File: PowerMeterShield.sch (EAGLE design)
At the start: 16 parts, among them IC1 MCP3426A0-E/SN, IC2 INA138

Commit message: Added DC-DC converter to isolate circuit; still missing optocouplers and differential voltage measurement
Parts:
- added DC1: VA-0505S, dc-dc-converter:VA-0505S
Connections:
- new net +5V: DC1.+VIN, JP3.4
- new net +5V/2: DC1.+VOUT
- new net GNDI: DC1.-VOUT
- net GND: now also DC1.-VIN
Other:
- moved on the sheet: JP3, JP4
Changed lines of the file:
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@@
 <attribute name="PRICE_10" value="1.21"/>
 </part>
-<part name="GND3" library="supply1" deviceset="GND" device=""/>
+<part name="GND3" library="supply1" deviceset="GNDI" device=""/>
 <part name="R4" library="rcl" deviceset="R-EU_" device="R0805" value="200k">
 <attribute name="OC_FARNELL" value="2129299"/>
@@
 <attribute name="PRICE_100" value="0.001"/>
 </part>
-<part name="GND1" library="supply1" deviceset="GND" device=""/>
+<part name="GND1" library="supply1" deviceset="GNDI" device=""/>
 <part name="X1" library="con-wago-500" deviceset="W237-102" device="">
 <attribute name="OC_FARNELL" value="1717001"/>
@@
 <attribute name="PRICE_10" value="2.06"/>
 </part>
-<part name="GND2" library="supply1" deviceset="GND" device=""/>
+<part name="GND2" library="supply1" deviceset="GNDI" device=""/>
 <part name="JP1" library="pinhead" deviceset="PINHD-1X10" device=""/>
 <part name="JP2" library="pinhead" deviceset="PINHD-1X8" device=""/>
@@
 <attribute name="PRICE_100" value="0.005"/>
 </part>
+<part name="DC1" library="dc-dc-converter" deviceset="VA-*?" device="S" technology="0505"/>
 </parts>
 <sheets>
@@
 <attribute name="PRICE_10" x="50.8" y="83.82" size="1.27" layer="96" display="off"/>
 </instance>
-<instance part="GND3" gate="1" x="68.58" y="60.96"/>
+<instance part="GND3" gate="G$1" x="68.58" y="60.96"/>
 <instance part="R4" gate="G$1" x="68.58" y="83.82" smashed="yes" rot="R90">
 <attribute name="OC_FARNELL" x="68.58" y="83.82" size="1.27" layer="96" rot="R90" display="off"/>
@@
 <attribute name="OC_FARNELL" x="58.42" y="66.04" size="1.27" layer="96" rot="R180" display="off"/>
 </instance>
-<instance part="GND1" gate="1" x="25.4" y="71.12"/>
+<instance part="GND1" gate="G$1" x="25.4" y="71.12"/>
 <instance part="X1" gate="-1" x="17.78" y="93.98">
 <attribute name="PRICE_10" x="17.78" y="93.98" size="1.27" layer="96" display="off"/>
@@
 <attribute name="PRICE_10" x="127" y="81.28" size="1.27" layer="96" display="off"/>
 </instance>
-<instance part="GND2" gate="1" x="93.98" y="60.96"/>
+<instance part="GND2" gate="G$1" x="93.98" y="60.96"/>
 <instance part="JP1" gate="A" x="160.02" y="195.58" rot="R90"/>
 <instance part="JP2" gate="A" x="193.04" y="195.58" rot="R90"/>
-<instance part="JP3" gate="A" x="157.48" y="149.86" rot="R270"/>
-<instance part="JP4" gate="A" x="185.42" y="149.86" rot="R270"/>
+<instance part="JP3" gate="A" x="157.48" y="132.08" rot="R270"/>
+<instance part="JP4" gate="A" x="185.42" y="132.08" rot="R270"/>
 <instance part="R1" gate="G$1" x="121.92" y="175.26" smashed="yes">
 <attribute name="OC_FARNELL" x="121.92" y="175.26" size="1.27" layer="96" display="off"/>
@@
 <attribute name="OC_FARNELL" x="101.6" y="88.9" size="1.27" layer="96" rot="R270" display="off"/>
 </instance>
+<instance part="DC1" gate="G$1" x="111.76" y="132.08" rot="R180"/>
 </instances>
 <busses>
@@
 <segment>
 <pinref part="IC2" gate="G$1" pin="V-"/>
-<pinref part="GND3" gate="1" pin="GND"/>
+<pinref part="GND3" gate="G$1" pin="GNDI"/>
 <wire x1="60.96" y1="76.2" x2="68.58" y2="76.2" width="0.1524" layer="91"/>
 <wire x1="68.58" y1="76.2" x2="68.58" y2="66.04" width="0.1524" layer="91"/>
@@
 <wire x1="25.4" y1="76.2" x2="25.4" y2="73.66" width="0.1524" layer="91"/>
 <junction x="25.4" y="76.2"/>
-<pinref part="GND1" gate="1" pin="GND"/>
+<pinref part="GND1" gate="G$1" pin="GNDI"/>
 <pinref part="X1" gate="-2" pin="KL"/>
 <pinref part="X2" gate="-2" pin="KL"/>
@@
 <junction x="93.98" y="66.04"/>
 <wire x1="93.98" y1="66.04" x2="93.98" y2="63.5" width="0.1524" layer="91"/>
-<pinref part="GND2" gate="1" pin="GND"/>
+<pinref part="GND2" gate="G$1" pin="GNDI"/>
 <wire x1="93.98" y1="76.2" x2="93.98" y2="81.28" width="0.1524" layer="91"/>
 <junction x="93.98" y="76.2"/>
@@
 <segment>
 <pinref part="JP3" gate="A" pin="3"/>
-<wire x1="162.56" y1="152.4" x2="162.56" y2="157.48" width="0.1524" layer="91"/>
+<wire x1="162.56" y1="134.62" x2="162.56" y2="139.7" width="0.1524" layer="91"/>
 <pinref part="JP3" gate="A" pin="2"/>
-<wire x1="165.1" y1="152.4" x2="165.1" y2="157.48" width="0.1524" layer="91"/>
-<wire x1="162.56" y1="157.48" x2="165.1" y2="157.48" width="0.1524" layer="91"/>
-<wire x1="165.1" y1="157.48" x2="165.1" y2="160.02" width="0.1524" layer="91"/>
-<junction x="165.1" y="157.48"/>
-<label x="165.1" y="160.02" size="1.27" layer="95" rot="R90" xref="yes"/>
+<wire x1="165.1" y1="134.62" x2="165.1" y2="139.7" width="0.1524" layer="91"/>
+<wire x1="162.56" y1="139.7" x2="165.1" y2="139.7" width="0.1524" layer="91"/>
+<wire x1="165.1" y1="139.7" x2="165.1" y2="142.24" width="0.1524" layer="91"/>
+<junction x="165.1" y="139.7"/>
+<label x="165.1" y="142.24" size="1.27" layer="95" rot="R90" xref="yes"/>
 </segment>
 <segment>
@@
 <wire x1="157.48" y1="193.04" x2="157.48" y2="187.96" width="0.1524" layer="91"/>
 <label x="157.48" y="187.96" size="1.27" layer="95" rot="R270" xref="yes"/>
+</segment>
+<segment>
+<pinref part="DC1" gate="G$1" pin="-VIN"/>
+<wire x1="124.46" y1="134.62" x2="127" y2="134.62" width="0.1524" layer="91"/>
+<label x="127" y="134.62" size="1.27" layer="95" xref="yes"/>
 </segment>
 </net>
@@
 <segment>
 <pinref part="JP3" gate="A" pin="7"/>
-<wire x1="152.4" y1="152.4" x2="152.4" y2="157.48" width="0.1524" layer="91"/>
-<label x="152.4" y="157.48" size="1.27" layer="95" rot="R90" xref="yes"/>
+<wire x1="152.4" y1="134.62" x2="152.4" y2="139.7" width="0.1524" layer="91"/>
+<label x="152.4" y="139.7" size="1.27" layer="95" rot="R90" xref="yes"/>
 </segment>
 <segment>
@@
 </segment>
 </net>
+<net name="+5V" class="0">
+<segment>
+<pinref part="JP3" gate="A" pin="4"/>
+<wire x1="160.02" y1="134.62" x2="160.02" y2="139.7" width="0.1524" layer="91"/>
+<label x="160.02" y="139.7" size="1.27" layer="95" rot="R90" xref="yes"/>
+</segment>
+<segment>
+<pinref part="DC1" gate="G$1" pin="+VIN"/>
+<wire x1="124.46" y1="129.54" x2="127" y2="129.54" width="0.1524" layer="91"/>
+<label x="127" y="129.54" size="1.27" layer="95" xref="yes"/>
+</segment>
+</net>
+<net name="GNDI" class="0">
+<segment>
+<pinref part="DC1" gate="G$1" pin="-VOUT"/>
+<wire x1="99.06" y1="134.62" x2="96.52" y2="134.62" width="0.1524" layer="91"/>
+<label x="96.52" y="134.62" size="1.27" layer="95" rot="R180" xref="yes"/>
+</segment>
+</net>
+<net name="+5V/2" class="0">
+<segment>
+<pinref part="DC1" gate="G$1" pin="+VOUT"/>
+<wire x1="99.06" y1="129.54" x2="96.52" y2="129.54" width="0.1524" layer="91"/>
+<label x="96.52" y="129.54" size="1.27" layer="95" rot="R180" xref="yes"/>
+</segment>
+</net>

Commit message: Added I²C isolation
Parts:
- added U1: ADUM1250ARZ, Adum1250:ADUM1250ARZ
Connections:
- new net SCLI: IC1.SCL, U1.SCL2
- new net SDAI: IC1.SDA, U1.SDA2
- net +5V/2: now also C1.1, IC1.VDD, IC2.V+, U1.VDD2
- net GND: now also U1.GND1; no longer C1.2, IC1.CH1-, IC1.CH2-, IC1.VSS, IC2.V-, R10.1, R4.1, X1-2.KL, X2-2.KL
- net GNDI: now also C1.2, IC1.CH1-, IC1.CH2-, IC1.VSS, IC2.V-, R10.1, R4.1, U1.GND2, X1-2.KL, X2-2.KL
- net IOREF: now also U1.VDD1; no longer C1.1, IC1.VDD, IC2.V+
- net SCL: now also U1.SCL1; no longer IC1.SCL
- net SDA: now also U1.SDA1; no longer IC1.SDA

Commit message: Added creepage distance of about 3mm for a bit of safety™
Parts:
- DC1: OC_FARNELL (none) -> 2079696
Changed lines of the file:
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@@
 <attribute name="PRICE_100" value="0.005"/>
 </part>
-<part name="DC1" library="dc-dc-converter" deviceset="VA-*?" device="S" technology="0505"/>
+<part name="DC1" library="dc-dc-converter" deviceset="VA-*?" device="S" technology="0505">
+<attribute name="OC_FARNELL" value="2079696"/>
+</part>
 <part name="U1" library="Adum1250" deviceset="ADUM1250ARZ" device=""/>
 </parts>

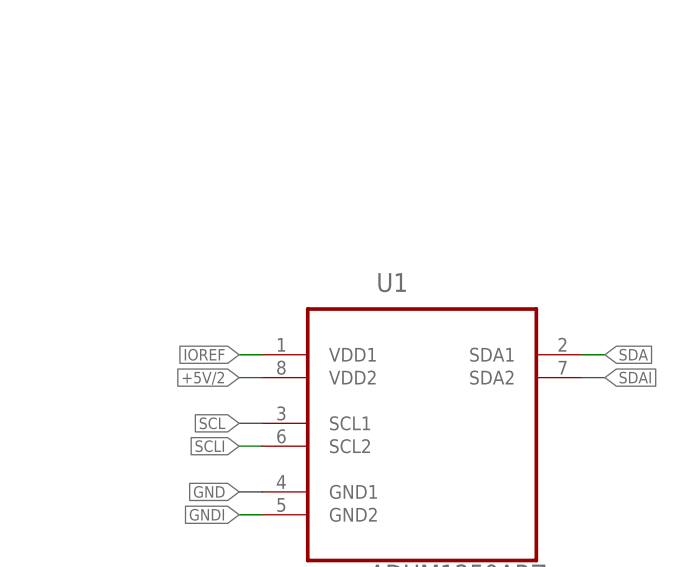
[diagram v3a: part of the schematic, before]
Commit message: Finalized design, made PCB larger in order to compensate for heigher components than the headers, so users can stack other shields on top of ours (hopefully).
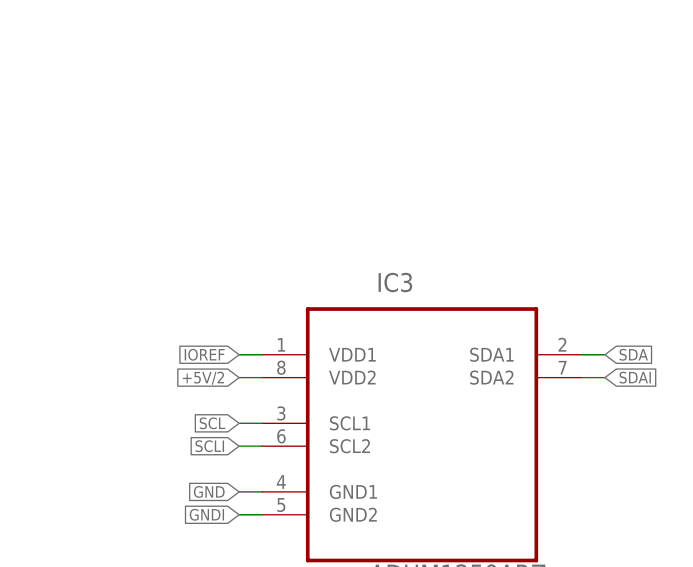
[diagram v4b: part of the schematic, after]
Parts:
- renumbered U1 to IC3
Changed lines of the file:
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@@
 <attribute name="PRICE_100" value="0.005"/>
 </part>
-<part name="DC1" library="dc-dc-converter" deviceset="VA-*?" device="S" technology="0505">
+<part name="DC1" library="dc-dc-converter" deviceset="VA-*?" device="S" technology="0505" value="VA-0505S">
 <attribute name="OC_FARNELL" value="2079696"/>
 </part>
-<part name="U1" library="Adum1250" deviceset="ADUM1250ARZ" device=""/>
+<part name="IC3" library="Adum1250" deviceset="ADUM1250ARZ" device=""/>
 </parts>
 <sheets>
@@
 </instance>
 <instance part="DC1" gate="G$1" x="111.76" y="132.08" rot="R180"/>
-<instance part="U1" gate="A" x="220.98" y="81.28"/>
+<instance part="IC3" gate="A" x="220.98" y="81.28"/>
 </instances>
 <busses>
@@
 </segment>
 <segment>
-<pinref part="U1" gate="A" pin="GND1"/>
+<pinref part="IC3" gate="A" pin="GND1"/>
 <wire x1="203.2" y1="71.12" x2="200.66" y2="71.12" width="0.1524" layer="91"/>
 <label x="200.66" y="71.12" size="1.27" layer="95" rot="R180" xref="yes"/>
@@
 </segment>
 <segment>
-<pinref part="U1" gate="A" pin="SCL1"/>
+<pinref part="IC3" gate="A" pin="SCL1"/>
 <wire x1="203.2" y1="78.74" x2="200.66" y2="78.74" width="0.1524" layer="91"/>
 <label x="200.66" y="78.74" size="1.27" layer="95" rot="R180" xref="yes"/>
@@
 </segment>
 <segment>
-<pinref part="U1" gate="A" pin="SDA1"/>
+<pinref part="IC3" gate="A" pin="SDA1"/>
 <wire x1="238.76" y1="86.36" x2="241.3" y2="86.36" width="0.1524" layer="91"/>
 <label x="241.3" y="86.36" size="1.27" layer="95" xref="yes"/>
@@
 </segment>
 <segment>
-<pinref part="U1" gate="A" pin="VDD1"/>
+<pinref part="IC3" gate="A" pin="VDD1"/>
 <wire x1="203.2" y1="86.36" x2="200.66" y2="86.36" width="0.1524" layer="91"/>
 <label x="200.66" y="86.36" size="1.27" layer="95" rot="R180" xref="yes"/>
@@
 </segment>
 <segment>
-<pinref part="U1" gate="A" pin="GND2"/>
+<pinref part="IC3" gate="A" pin="GND2"/>
 <wire x1="203.2" y1="68.58" x2="200.66" y2="68.58" width="0.1524" layer="91"/>
 <label x="200.66" y="68.58" size="1.27" layer="95" rot="R180" xref="yes"/>
@@
 </segment>
 <segment>
-<pinref part="U1" gate="A" pin="VDD2"/>
+<pinref part="IC3" gate="A" pin="VDD2"/>
 <wire x1="203.2" y1="83.82" x2="200.66" y2="83.82" width="0.1524" layer="91"/>
 <label x="200.66" y="83.82" size="1.27" layer="95" rot="R180" xref="yes"/>
@@
 </segment>
 <segment>
-<pinref part="U1" gate="A" pin="SDA2"/>
+<pinref part="IC3" gate="A" pin="SDA2"/>
 <wire x1="238.76" y1="83.82" x2="241.3" y2="83.82" width="0.1524" layer="91"/>
 <label x="241.3" y="83.82" size="1.27" layer="95" xref="yes"/>
@@
 </segment>
 <segment>
-<pinref part="U1" gate="A" pin="SCL2"/>
+<pinref part="IC3" gate="A" pin="SCL2"/>
 <wire x1="203.2" y1="76.2" x2="200.66" y2="76.2" width="0.1524" layer="91"/>
 <label x="200.66" y="76.2" size="1.27" layer="95" rot="R180" xref="yes"/>

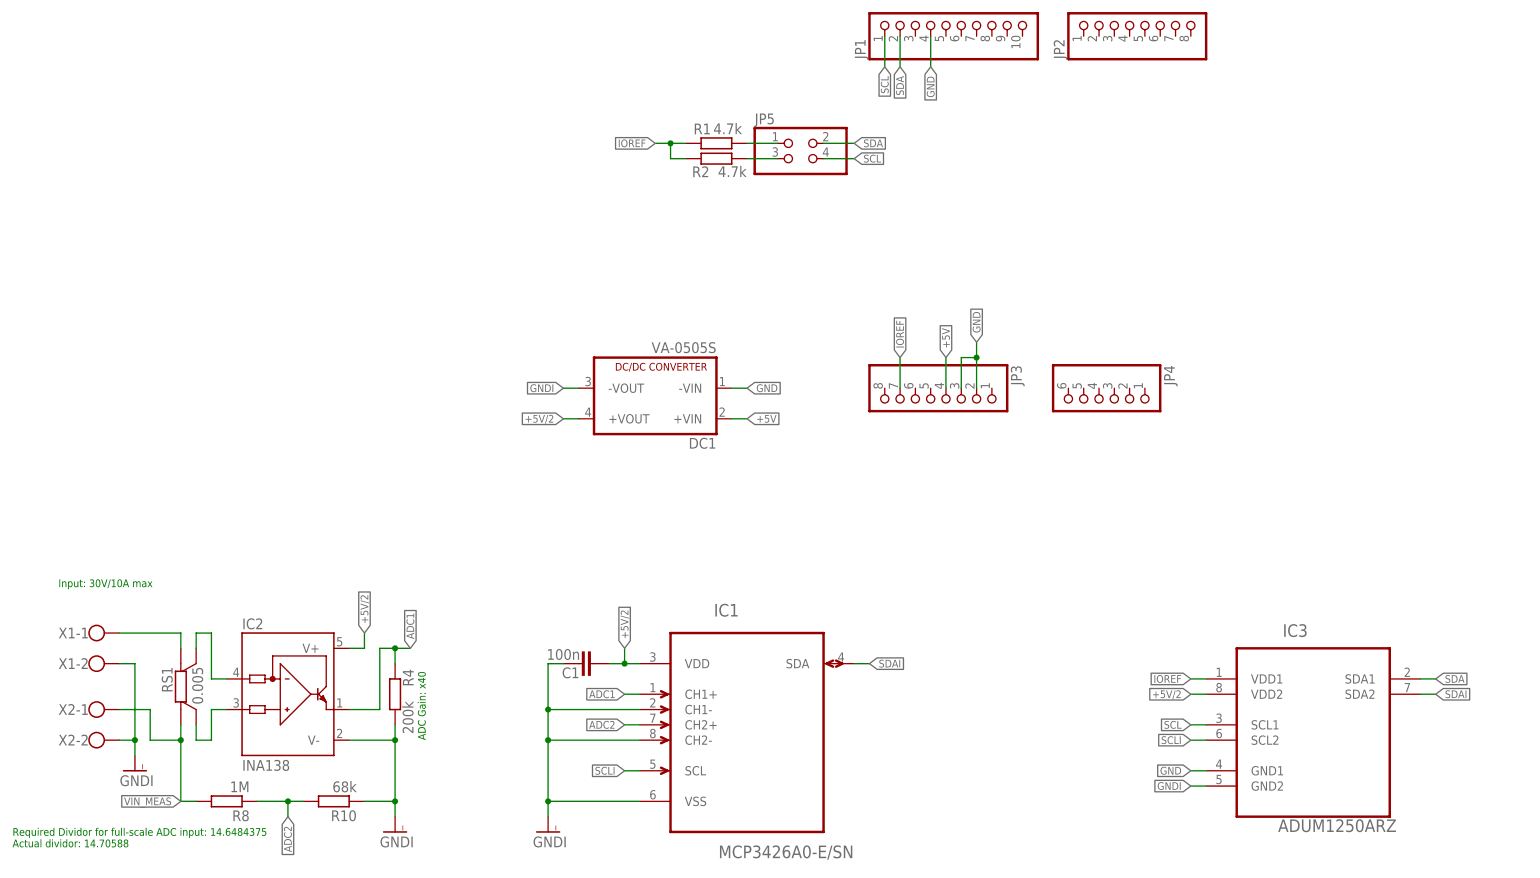
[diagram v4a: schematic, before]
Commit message: Added port names to silkscreen, added I²C pullups for the internal I²C bus
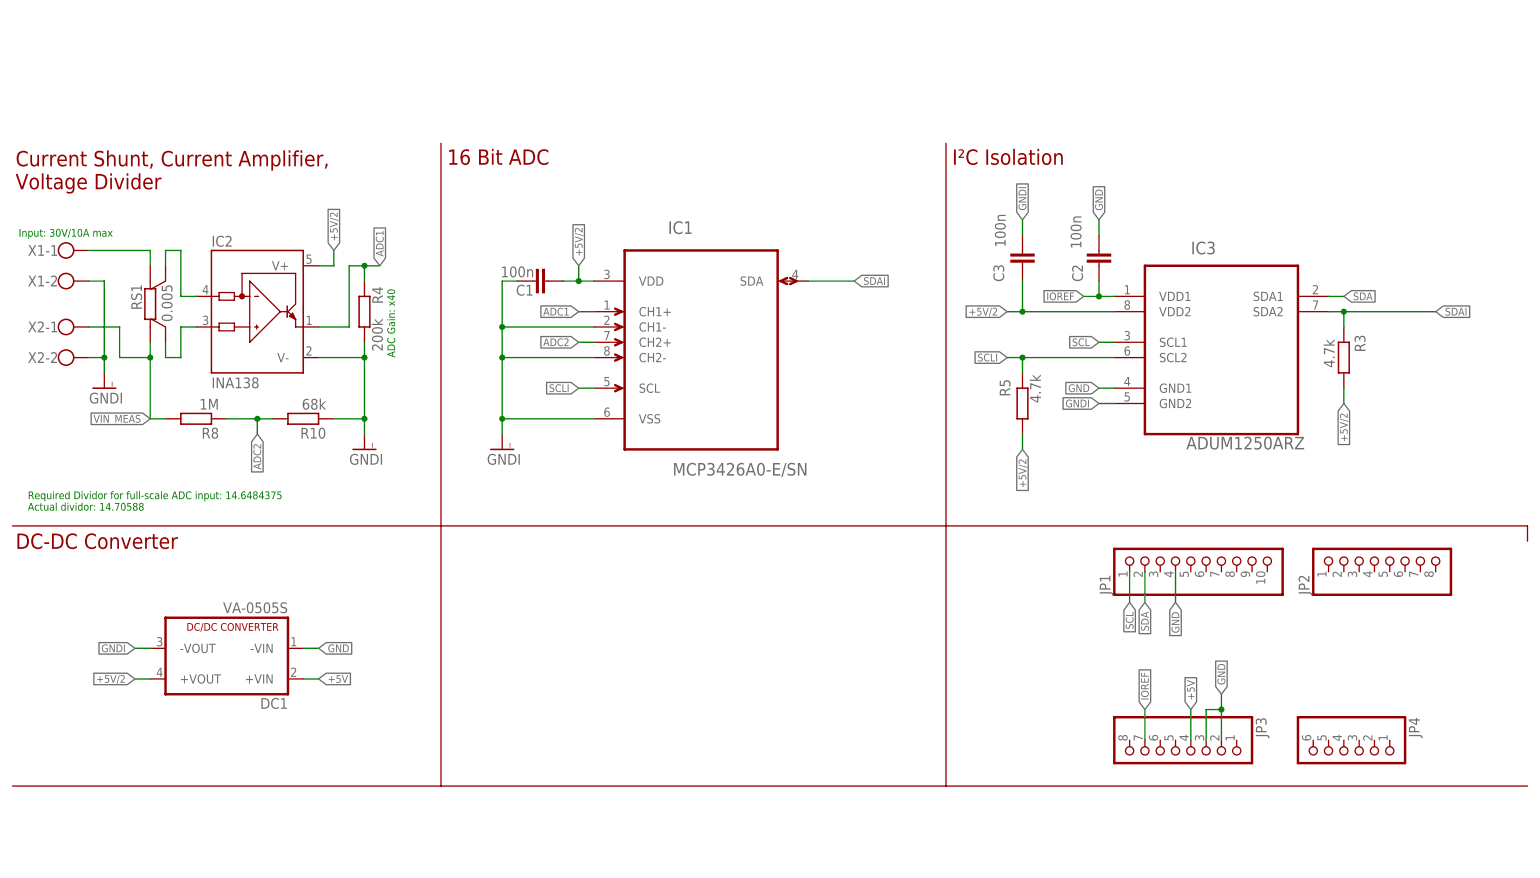
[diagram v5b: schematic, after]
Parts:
- removed JP5: (no value), pinhead:PINHD-2X2
- removed R1, R2: 4.7k, rcl:R-EU_R0805
- added C2, C3: 100n, rcl:C-EUC0805
- added R3, R5: 4.7k, rcl:R-EU_R0805
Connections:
- removed net N$3: JP5.1, R1.2
- removed net N$4: JP5.3, R2.2
- net +5V/2: now also C3.1, R3.2, R5.2
- net GND: now also C2.2
- net GNDI: now also C3.2
- net IOREF: now also C2.1; no longer R1.1, R2.1
- net SCL: no longer JP5.4
- net SCLI: now also R5.1
- net SDA: no longer JP5.2
- net SDAI: now also R3.1
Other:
- note added: "16 Bit ADC"
- note added: "Current Shunt, Current Amplifier, Voltage Divider"
- note added: "DC-DC Converter"
- note added: "I²C Isolation"
- moved on the sheet: C1, DC1, IC1, IC2, IC3, JP1, JP2, JP3, JP4, R10, R4, R8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
